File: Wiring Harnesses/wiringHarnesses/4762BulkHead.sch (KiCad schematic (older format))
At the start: 0 parts

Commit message: Added some bulkheads and internal HV connectors
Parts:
- added J?: PAVE_4762, symbol connectors:PAVE_4762
- added J? (x2): Anderson_Female, symbol Connector:Conn_01x02_Female
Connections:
- net labels added: CAN_HI, CAN_LO, CHARGE, GND, HP_12V, LP_12V, READY, RXD, Shield, TXD, ~PROG_EN
- wire segments 0 -> 30
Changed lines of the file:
@@
 $Descr A4 11693 8268
 encoding utf-8
-Sheet 1 20
+Sheet 13 20
 Title ""
 Date ""
@@
 Comment4 ""
 $EndDescr
+$Comp
+L connectors:PAVE_4762 J?
+U 1 1 5CD609CA
+P 5650 3900
+F 0 "J?" H 5140 4770 79  0000 C CNN
+F 1 "PAVE_4762" H 5180 4620 79  0000 C CNN
+F 2 "" V 5250 3350 79  0001 C CNN
+F 3 "" V 5250 3350 79  0001 C CNN
+	1    5650 3900
+	1    0    0    -1
+$EndComp
+Wire Notes Line
+	5650 1470 5650 6330
+Wire Wire Line
+	5350 4200 4500 4200
+Text Label 4600 4200 0    50   ~ 0
+GND
+Text Label 4600 4100 0    50   ~ 0
+HP_12V
+Wire Wire Line
+	5350 4100 4500 4100
+Text Label 4600 3900 0    50   ~ 0
+LP_12V
+Wire Wire Line
+	5350 3800 4500 3800
+Text Label 4600 3800 0    50   ~ 0
+CHARGE
+Wire Wire Line
+	5350 3700 4500 3700
+Text Label 4600 3700 0    50   ~ 0
+READY
+Wire Wire Line
+	5350 3500 4500 3500
+Text Label 4600 3500 0    50   ~ 0
+CAN_LO
+Wire Wire Line
+	5350 3400 4500 3400
+Text Label 4600 3400 0    50   ~ 0
+CAN_HI
+Wire Wire Line
+	5350 3600 4500 3600
+Text Label 4600 3600 0    50   ~ 0
+Shield
+Wire Wire Line
+	5350 3900 4500 3900
+Wire Wire Line
+	5350 4000 4500 4000
+Text Label 4600 4000 0    50   ~ 0
+GND
+Wire Wire Line
+	5350 4300 4500 4300
+Text Label 4600 4300 0    50   ~ 0
+TXD
+Wire Wire Line
+	5350 4400 4500 4400
+Text Label 4600 4400 0    50   ~ 0
+RXD
+Wire Wire Line
+	5350 4500 4500 4500
+Text Label 4600 4500 0    50   ~ 0
+~PROG_EN
+Text Label 6700 4200 2    50   ~ 0
+GND
+Text Label 6700 4100 2    50   ~ 0
+HP_12V
+Text Label 6700 3900 2    50   ~ 0
+LP_12V
+Text Label 6700 3800 2    50   ~ 0
+CHARGE
+Text Label 6700 3700 2    50   ~ 0
+READY
+Text Label 6700 3500 2    50   ~ 0
+CAN_LO
+Text Label 6700 3400 2    50   ~ 0
+CAN_HI
+Text Label 6700 3600 2    50   ~ 0
+Shield
+Text Label 6700 4000 2    50   ~ 0
+GND
+Wire Wire Line
+	5950 4300 6800 4300
+Text Label 6700 4300 2    50   ~ 0
+TXD
+Wire Wire Line
+	5950 4400 6800 4400
+Text Label 6700 4400 2    50   ~ 0
+RXD
+Wire Wire Line
+	5950 4500 6800 4500
+Text Label 6700 4500 2    50   ~ 0
+~PROG_EN
+$Comp
+L Connector:Conn_01x02_Female J?
+U 1 1 5CD67CB3
+P 8350 3900
+F 0 "J?" H 8378 3876 50  0000 L CNN
+F 1 "Anderson_Female" H 8378 3785 50  0000 L CNN
+F 2 "" H 8350 3900 50  0001 C CNN
+F 3 "~" H 8350 3900 50  0001 C CNN
+	1    8350 3900
+	1    0    0    -1
+$EndComp
+$Comp
+L Connector:Conn_01x02_Female J?
+U 1 1 5CD6857B
+P 7400 4100
+F 0 "J?" H 7428 4076 50  0000 L CNN
+F 1 "Anderson_Female" H 7428 3985 50  0000 L CNN
+F 2 "" H 7400 4100 50  0001 C CNN
+F 3 "~" H 7400 4100 50  0001 C CNN
+	1    7400 4100
+	1    0    0    -1
+$EndComp
+Wire Wire Line
+	5950 4100 7200 4100
+Wire Wire Line
+	5950 4200 7200 4200
+Wire Wire Line
+	7150 3400 7150 3100
+Wire Wire Line
+	7150 3100 7500 3100
+Wire Wire Line
+	5950 3400 7150 3400
+Wire Wire Line
+	7250 3500 7250 3200
+Wire Wire Line
+	7250 3200 7500 3200
+Wire Wire Line
+	5950 3500 7250 3500
+Wire Wire Line
+	7350 3600 7350 3300
+Wire Wire Line
+	7350 3300 7500 3300
+Wire Wire Line
+	5950 3600 7350 3600
+Wire Wire Line
+	5950 3700 7350 3700
+Wire Wire Line
+	5950 3900 8150 3900
+Wire Wire Line
+	5950 4000 8150 4000
+Wire Wire Line
+	5950 3800 7350 3800
 $EndSCHEMATC

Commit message: minor changes
bulkheads
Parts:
- J?: symbol connectors:PAVE_4762 -> wiringHarnesses-rescue:PAVE_4762-connectors
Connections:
- net labels added: 800V_PASS, HVGND_PASS, SPARE
- net labels removed: RXD, TXD, ~PROG_EN
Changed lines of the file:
@@
 $EndDescr
 $Comp
-L connectors:PAVE_4762 J?
+L wiringHarnesses-rescue:PAVE_4762-connectors J?
 U 1 1 5CD609CA
 P 5650 3900
@@
 	5350 4300 4500 4300
 Text Label 4600 4300 0    50   ~ 0
-TXD
+800V_PASS
 Wire Wire Line
 	5350 4400 4500 4400
 Text Label 4600 4400 0    50   ~ 0
-RXD
+HVGND_PASS
 Wire Wire Line
 	5350 4500 4500 4500
-Text Label 4600 4500 0    50   ~ 0
-~PROG_EN
 Text Label 6700 4200 2    50   ~ 0
 GND
@@
 Text Label 6700 4000 2    50   ~ 0
 GND
-Wire Wire Line
-	5950 4300 6800 4300
-Text Label 6700 4300 2    50   ~ 0
-TXD
-Wire Wire Line
-	5950 4400 6800 4400
-Text Label 6700 4400 2    50   ~ 0
-RXD
-Wire Wire Line
-	5950 4500 6800 4500
-Text Label 6700 4500 2    50   ~ 0
-~PROG_EN
 $Comp
 L Connector:Conn_01x02_Female J?
@@
 Wire Wire Line
 	5950 3800 7350 3800
+Wire Wire Line
+	5950 4500 6800 4500
+Text Label 6700 4400 2    50   ~ 0
+HVGND_PASS
+Wire Wire Line
+	5950 4400 6800 4400
+Text Label 6700 4300 2    50   ~ 0
+800V_PASS
+Wire Wire Line
+	5950 4300 6800 4300
+Text Label 4600 4500 0    50   ~ 0
+SPARE
+Text Label 6200 4500 0    50   ~ 0
+SPARE
 $EndSCHEMATC

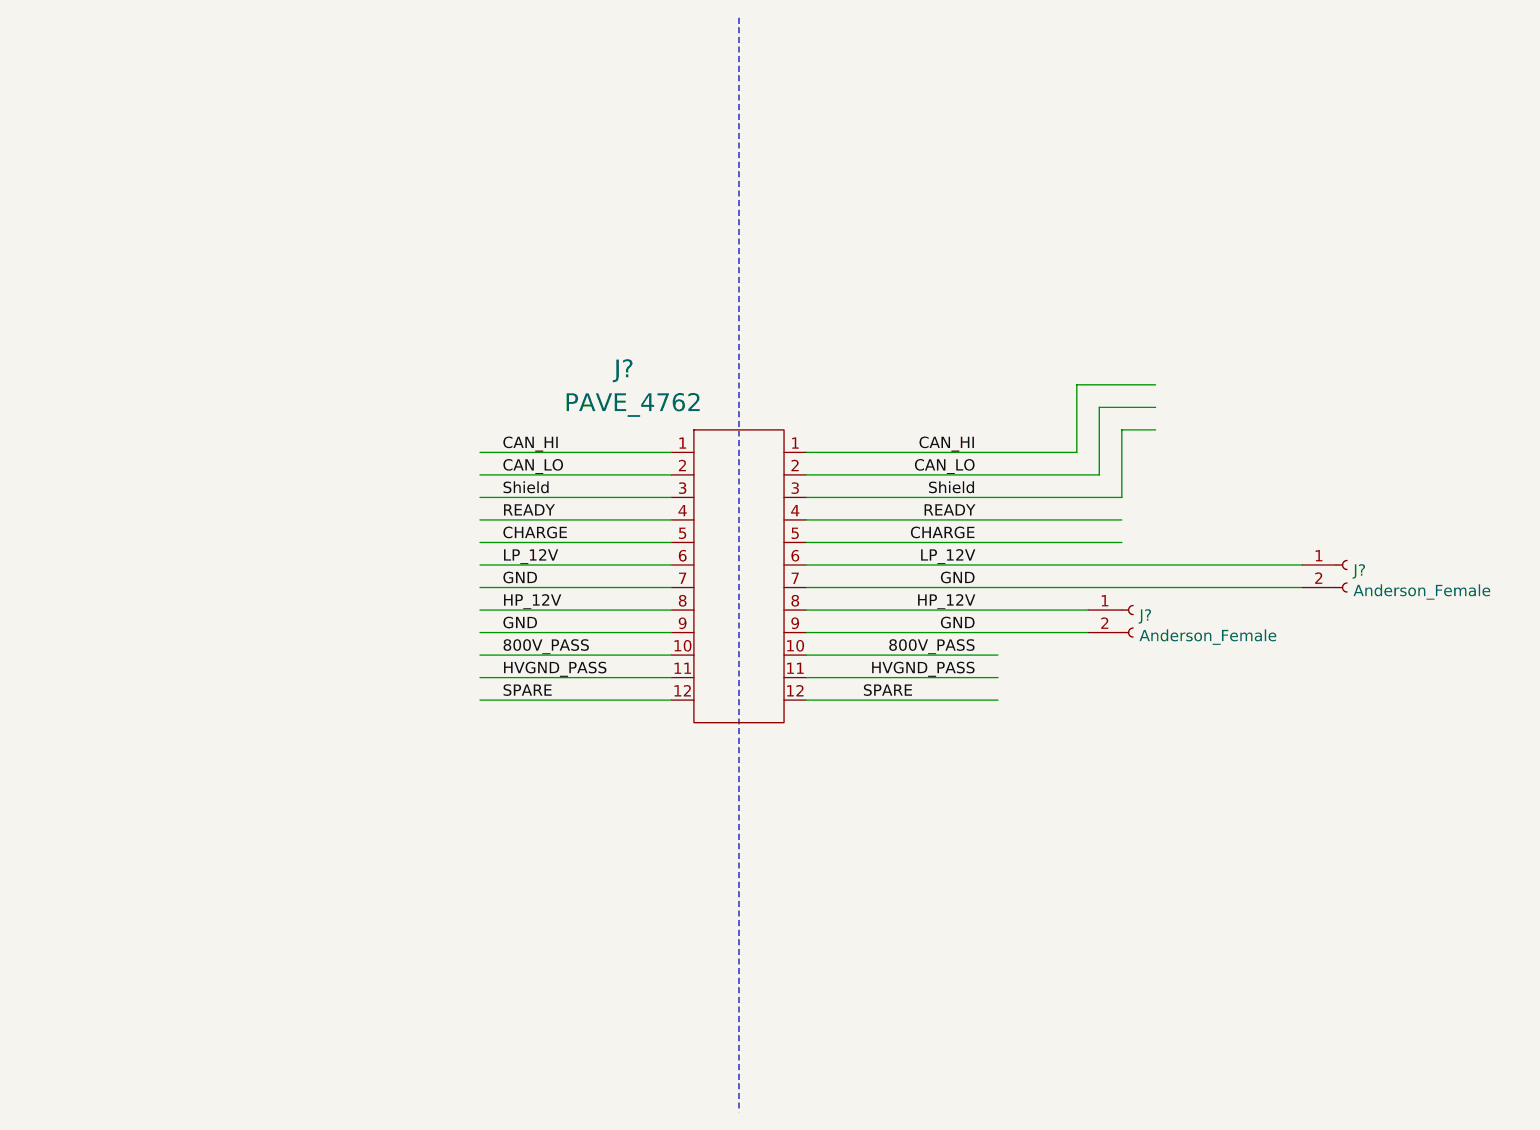
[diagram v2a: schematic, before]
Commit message: added 1872 bulkhead
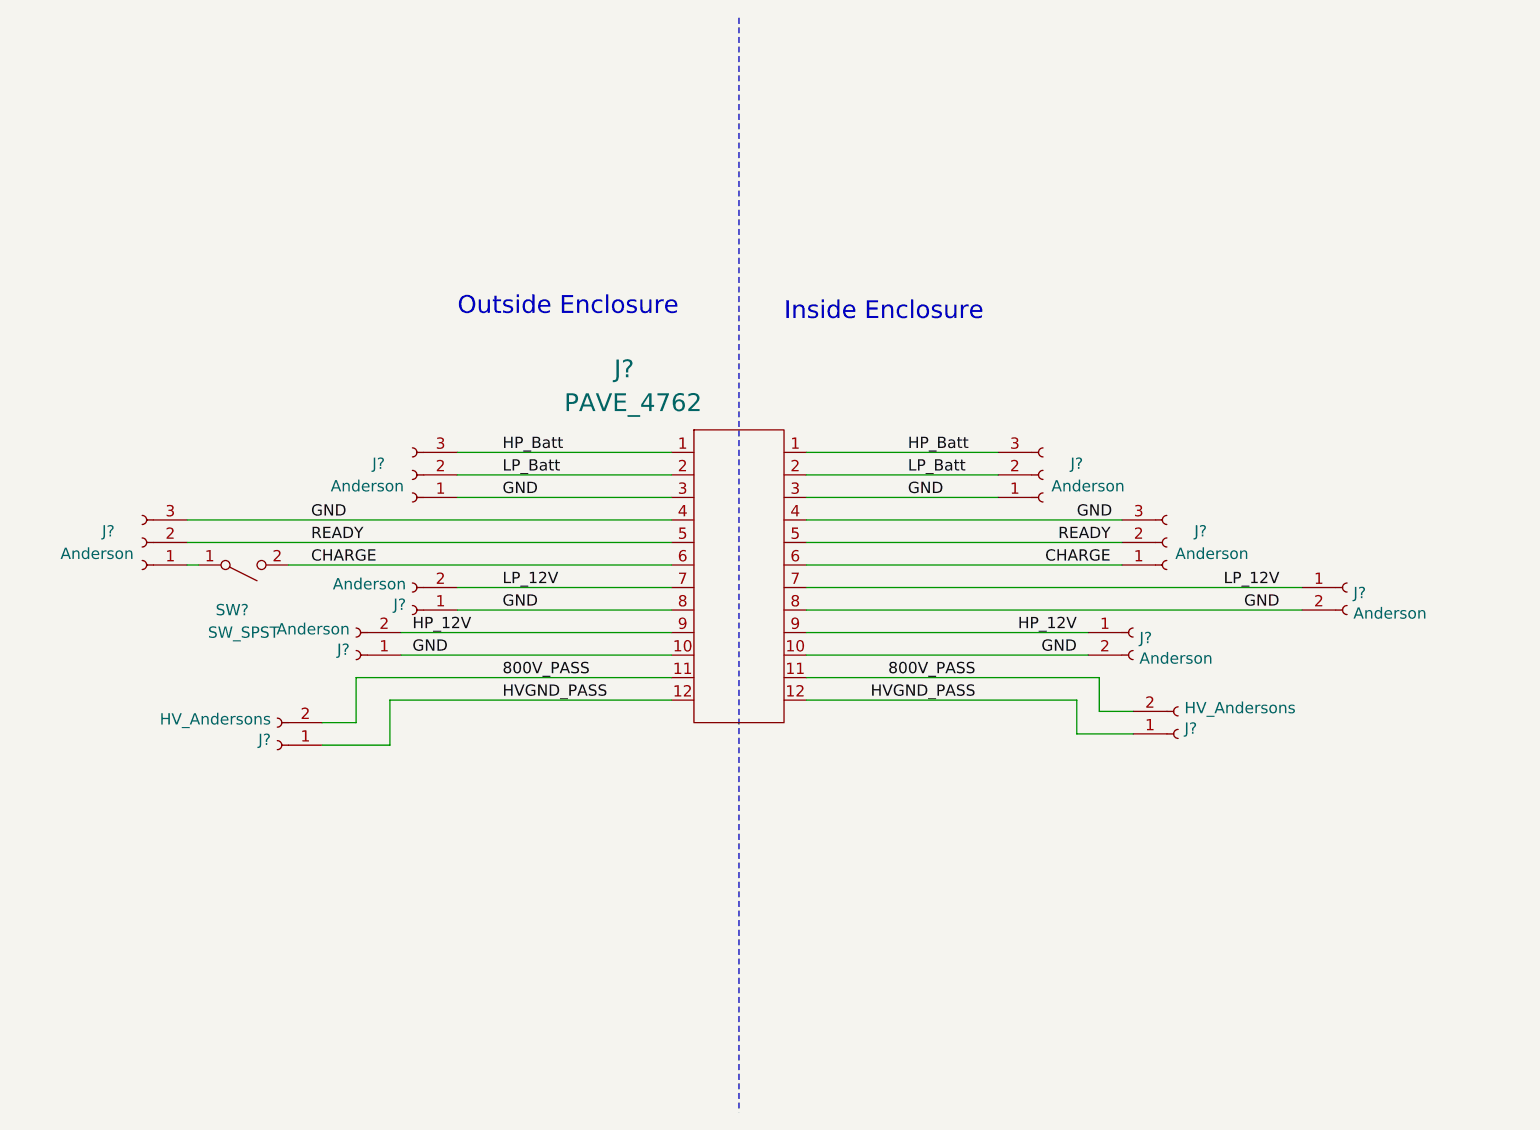
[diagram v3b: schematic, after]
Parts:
- added J? (x2): Anderson, symbol Connector:Conn_01x02_Female
- added J? (x4): Anderson, symbol Connector:Conn_01x03_Female
- added J? (x2): HV_Andersons, symbol Connector:Conn_01x02_Female
- added SW?: SW_SPST, symbol Switch:SW_SPST
- J? (x2): value Anderson_Female -> Anderson
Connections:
- net labels added: HP_Batt, LP_Batt
- net labels removed: CAN_HI, CAN_LO, SPARE, Shield
- wire segments 30 -> 33
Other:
- note added: "Inside Enclosure\n\n"
- note added: "Outside Enclosure\n"
- moved on the sheet: J?
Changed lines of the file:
@@
 $Descr A4 11693 8268
 encoding utf-8
-Sheet 13 20
+Sheet 12 20
 Title ""
 Date ""
@@
 Wire Notes Line
 	5650 1470 5650 6330
-Wire Wire Line
-	5350 4200 4500 4200
-Text Label 4600 4200 0    50   ~ 0
-GND
+Text Label 4200 4300 0    50   ~ 0
+GND
+Text Label 4200 4200 0    50   ~ 0
+HP_12V
+Text Label 4600 4000 0    50   ~ 0
+LP_12V
+Text Label 3750 3900 0    50   ~ 0
+CHARGE
+Text Label 3750 3800 0    50   ~ 0
+READY
 Text Label 4600 4100 0    50   ~ 0
+GND
+Text Label 4600 4400 0    50   ~ 0
+800V_PASS
+Text Label 4600 4500 0    50   ~ 0
+HVGND_PASS
+Text Label 7150 4300 2    50   ~ 0
+GND
+Text Label 7150 4200 2    50   ~ 0
 HP_12V
-Wire Wire Line
-	5350 4100 4500 4100
-Text Label 4600 3900 0    50   ~ 0
+Text Label 8050 4000 2    50   ~ 0
 LP_12V
-Wire Wire Line
-	5350 3800 4500 3800
-Text Label 4600 3800 0    50   ~ 0
+Text Label 7300 3900 2    50   ~ 0
 CHARGE
-Wire Wire Line
-	5350 3700 4500 3700
-Text Label 4600 3700 0    50   ~ 0
+Text Label 7300 3800 2    50   ~ 0
 READY
-Wire Wire Line
-	5350 3500 4500 3500
+Text Label 8050 4100 2    50   ~ 0
+GND
+$Comp
+L Connector:Conn_01x02_Female J?
+U 1 1 5CD67CB3
+P 8350 4000
+F 0 "J?" H 8378 3976 50  0000 L CNN
+F 1 "Anderson" H 8378 3885 50  0000 L CNN
+F 2 "" H 8350 4000 50  0001 C CNN
+F 3 "~" H 8350 4000 50  0001 C CNN
+	1    8350 4000
+	1    0    0    -1
+$EndComp
+$Comp
+L Connector:Conn_01x02_Female J?
+U 1 1 5CD6857B
+P 7400 4200
+F 0 "J?" H 7428 4176 50  0000 L CNN
+F 1 "Anderson" H 7428 4085 50  0000 L CNN
+F 2 "" H 7400 4200 50  0001 C CNN
+F 3 "~" H 7400 4200 50  0001 C CNN
+	1    7400 4200
+	1    0    0    -1
+$EndComp
+Wire Wire Line
+	5950 4200 7200 4200
+Wire Wire Line
+	5950 4300 7200 4300
+Wire Wire Line
+	5950 3800 7350 3800
+Wire Wire Line
+	5950 4000 8150 4000
+Wire Wire Line
+	5950 4100 8150 4100
+Wire Wire Line
+	5950 3900 7350 3900
+Wire Wire Line
+	5950 3600 6800 3600
+Text Label 6700 4500 2    50   ~ 0
+HVGND_PASS
+Text Label 6700 4400 2    50   ~ 0
+800V_PASS
+Text Label 4600 3600 0    50   ~ 0
+GND
+Text Label 6400 3600 0    50   ~ 0
+GND
+Text Label 3750 3700 0    50   ~ 0
+GND
 Text Label 4600 3500 0    50   ~ 0
-CAN_LO
-Wire Wire Line
-	5350 3400 4500 3400
+LP_Batt
 Text Label 4600 3400 0    50   ~ 0
-CAN_HI
-Wire Wire Line
-	5350 3600 4500 3600
-Text Label 4600 3600 0    50   ~ 0
-Shield
-Wire Wire Line
-	5350 3900 4500 3900
-Wire Wire Line
-	5350 4000 4500 4000
-Text Label 4600 4000 0    50   ~ 0
-GND
-Wire Wire Line
-	5350 4300 4500 4300
-Text Label 4600 4300 0    50   ~ 0
-800V_PASS
-Wire Wire Line
-	5350 4400 4500 4400
-Text Label 4600 4400 0    50   ~ 0
-HVGND_PASS
-Wire Wire Line
-	5350 4500 4500 4500
-Text Label 6700 4200 2    50   ~ 0
-GND
-Text Label 6700 4100 2    50   ~ 0
-HP_12V
-Text Label 6700 3900 2    50   ~ 0
-LP_12V
-Text Label 6700 3800 2    50   ~ 0
-CHARGE
-Text Label 6700 3700 2    50   ~ 0
-READY
-Text Label 6700 3500 2    50   ~ 0
-CAN_LO
-Text Label 6700 3400 2    50   ~ 0
-CAN_HI
-Text Label 6700 3600 2    50   ~ 0
-Shield
-Text Label 6700 4000 2    50   ~ 0
-GND
-$Comp
-L Connector:Conn_01x02_Female J?
-U 1 1 5CD67CB3
-P 8350 3900
-F 0 "J?" H 8378 3876 50  0000 L CNN
-F 1 "Anderson_Female" H 8378 3785 50  0000 L CNN
-F 2 "" H 8350 3900 50  0001 C CNN
-F 3 "~" H 8350 3900 50  0001 C CNN
-	1    8350 3900
-	1    0    0    -1
-$EndComp
-$Comp
-L Connector:Conn_01x02_Female J?
-U 1 1 5CD6857B
-P 7400 4100
-F 0 "J?" H 7428 4076 50  0000 L CNN
-F 1 "Anderson_Female" H 7428 3985 50  0000 L CNN
-F 2 "" H 7400 4100 50  0001 C CNN
-F 3 "~" H 7400 4100 50  0001 C CNN
-	1    7400 4100
-	1    0    0    -1
-$EndComp
-Wire Wire Line
-	5950 4100 7200 4100
-Wire Wire Line
-	5950 4200 7200 4200
-Wire Wire Line
-	7150 3400 7150 3100
-Wire Wire Line
-	7150 3100 7500 3100
-Wire Wire Line
-	5950 3400 7150 3400
-Wire Wire Line
-	7250 3500 7250 3200
-Wire Wire Line
-	7250 3200 7500 3200
-Wire Wire Line
-	5950 3500 7250 3500
-Wire Wire Line
-	7350 3600 7350 3300
-Wire Wire Line
-	7350 3300 7500 3300
-Wire Wire Line
-	5950 3600 7350 3600
+HP_Batt
+Wire Wire Line
+	5950 3400 6800 3400
+Wire Wire Line
+	5950 3500 6800 3500
+Text Label 6400 3400 0    50   ~ 0
+HP_Batt
+Text Label 6400 3500 0    50   ~ 0
+LP_Batt
+Text Label 7150 3700 0    50   ~ 0
+GND
+Text Notes 4400 2800 0    79   ~ 0
+Outside Enclosure\n
+Text Notes 5850 2950 0    79   ~ 0
+Inside Enclosure\n\n
+$Comp
+L Connector:Conn_01x02_Female J?
+U 1 1 5D0C44EB
+P 3950 4300
+F 0 "J?" H 3978 4276 50  0000 L CNN
+F 1 "Anderson" H 3978 4185 50  0000 L CNN
+F 2 "" H 3950 4300 50  0001 C CNN
+F 3 "~" H 3950 4300 50  0001 C CNN
+	1    3950 4300
+	-1   0    0    1
+$EndComp
+Wire Wire Line
+	4150 4200 5350 4200
+Wire Wire Line
+	4150 4300 5350 4300
+$Comp
+L Connector:Conn_01x02_Female J?
+U 1 1 5D0C510C
+P 4200 4100
+F 0 "J?" H 4228 4076 50  0000 L CNN
+F 1 "Anderson" H 4228 3985 50  0000 L CNN
+F 2 "" H 4200 4100 50  0001 C CNN
+F 3 "~" H 4200 4100 50  0001 C CNN
+	1    4200 4100
+	-1   0    0    1
+$EndComp
+Wire Wire Line
+	4400 4100 5350 4100
+Wire Wire Line
+	4400 4000 5350 4000
+$Comp
+L Connector:Conn_01x03_Female J?
+U 1 1 5D0C6DC9
+P 3000 3800
+F 0 "J?" H 3150 3750 50  0000 C CNN
+F 1 "Anderson" H 3200 3850 50  0000 C CNN
+F 2 "" H 3000 3800 50  0001 C CNN
+F 3 "~" H 3000 3800 50  0001 C CNN
+	1    3000 3800
+	-1   0    0    1
+$EndComp
+$Comp
+L Switch:SW_SPST SW?
+U 1 1 5D0C944E
+P 3450 3900
+F 0 "SW?" H 3400 4100 50  0000 C CNN
+F 1 "SW_SPST" H 3450 4200 50  0000 C CNN
+F 2 "" H 3450 3900 50  0001 C CNN
+F 3 "" H 3450 3900 50  0001 C CNN
+	1    3450 3900
+	1    0    0    1
+$EndComp
+Wire Wire Line
+	3200 3900 3250 3900
+Wire Wire Line
+	3650 3900 5350 3900
+Wire Wire Line
+	3200 3800 5350 3800
+$Comp
+L Connector:Conn_01x03_Female J?
+U 1 1 5D0CEB5E
+P 7550 3800
+F 0 "J?" H 7700 3750 50  0000 C CNN
+F 1 "Anderson" H 7750 3850 50  0000 C CNN
+F 2 "" H 7550 3800 50  0001 C CNN
+F 3 "~" H 7550 3800 50  0001 C CNN
+	1    7550 3800
+	1    0    0    1
+$EndComp
+$Comp
+L Connector:Conn_01x02_Female J?
+U 1 1 5D0D11C4
+P 3600 4700
+F 0 "J?" H 3628 4676 50  0000 L CNN
+F 1 "HV_Andersons" H 3628 4585 50  0000 L CNN
+F 2 "" H 3600 4700 50  0001 C CNN
+F 3 "~" H 3600 4700 50  0001 C CNN
+	1    3600 4700
+	-1   0    0    1
+$EndComp
+Wire Wire Line
+	4100 4500 4100 4700
+Wire Wire Line
+	4100 4700 3800 4700
+Wire Wire Line
+	4100 4500 5350 4500
+Wire Wire Line
+	3800 4600 3950 4600
+Wire Wire Line
+	3950 4600 3950 4400
+Wire Wire Line
+	3950 4400 5350 4400
+$Comp
+L Connector:Conn_01x02_Female J?
+U 1 1 5D0D2374
+P 7600 4650
+F 0 "J?" H 7628 4626 50  0000 L CNN
+F 1 "HV_Andersons" H 7628 4535 50  0000 L CNN
+F 2 "" H 7600 4650 50  0001 C CNN
+F 3 "~" H 7600 4650 50  0001 C CNN
+	1    7600 4650
+	1    0    0    1
+$EndComp
+Wire Wire Line
+	7150 4500 7150 4650
+Wire Wire Line
+	7150 4650 7400 4650
+Wire Wire Line
+	5950 4500 7150 4500
+Wire Wire Line
+	7400 4550 7250 4550
+Wire Wire Line
+	7250 4550 7250 4400
+Wire Wire Line
+	5950 4400 7250 4400
+Wire Wire Line
+	5350 3600 4400 3600
+Wire Wire Line
+	4400 3500 5350 3500
+Wire Wire Line
+	4400 3400 5350 3400
+$Comp
+L Connector:Conn_01x03_Female J?
+U 1 1 5D0D8D86
+P 4200 3500
+F 0 "J?" H 4350 3450 50  0000 C CNN
+F 1 "Anderson" H 4400 3550 50  0000 C CNN
+F 2 "" H 4200 3500 50  0001 C CNN
+F 3 "~" H 4200 3500 50  0001 C CNN
+	1    4200 3500
+	-1   0    0    1
+$EndComp
+Wire Wire Line
+	3200 3700 5350 3700
+$Comp
+L Connector:Conn_01x03_Female J?
+U 1 1 5D0DBA70
+P 7000 3500
+F 0 "J?" H 7150 3450 50  0000 C CNN
+F 1 "Anderson" H 7200 3550 50  0000 C CNN
+F 2 "" H 7000 3500 50  0001 C CNN
+F 3 "~" H 7000 3500 50  0001 C CNN
+	1    7000 3500
+	1    0    0    1
+$EndComp
 Wire Wire Line
 	5950 3700 7350 3700
-Wire Wire Line
-	5950 3900 8150 3900
-Wire Wire Line
-	5950 4000 8150 4000
-Wire Wire Line
-	5950 3800 7350 3800
-Wire Wire Line
-	5950 4500 6800 4500
-Text Label 6700 4400 2    50   ~ 0
-HVGND_PASS
-Wire Wire Line
-	5950 4400 6800 4400
-Text Label 6700 4300 2    50   ~ 0
-800V_PASS
-Wire Wire Line
-	5950 4300 6800 4300
-Text Label 4600 4500 0    50   ~ 0
-SPARE
-Text Label 6200 4500 0    50   ~ 0
-SPARE
 $EndSCHEMATC
